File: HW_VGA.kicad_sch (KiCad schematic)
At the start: 3 parts, among them U1 25.175 MHz, U301 GAL22V10

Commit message: start working on VRAM/read logic
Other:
- added sheet ReadVRAM (ReadVRAM.kicad_sch)
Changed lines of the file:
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@@
+	)
+	(sheet
+		(at 93.98 116.84)
+		(size 27.94 45.72)
+		(fields_autoplaced yes)
+		(stroke
+			(width 0.1524)
+			(type solid)
+		)
+		(fill
+			(color 0 0 0 0.0000)
+		)
+		(property "Sheetname" "ReadVRAM"
+			(at 93.98 116.1284 0)
+			(effects
+				(font
+					(size 1.27 1.27)
+				)
+				(justify left bottom)
+			)
+		)
+		(property "Sheetfile" "ReadVRAM.kicad_sch"
+			(at 93.98 163.1446 0)
+			(effects
+				(font
+					(size 1.27 1.27)
+				)
+				(justify left top)
+			)
+		)
+		(instances
+			(project "HW_VGA"
+				(path "/c4bd4b39-993a-4195-805f-b4de6fa4aea5"
+					(page "7")
+				)
+			)
+		)
 	)
 	(sheet

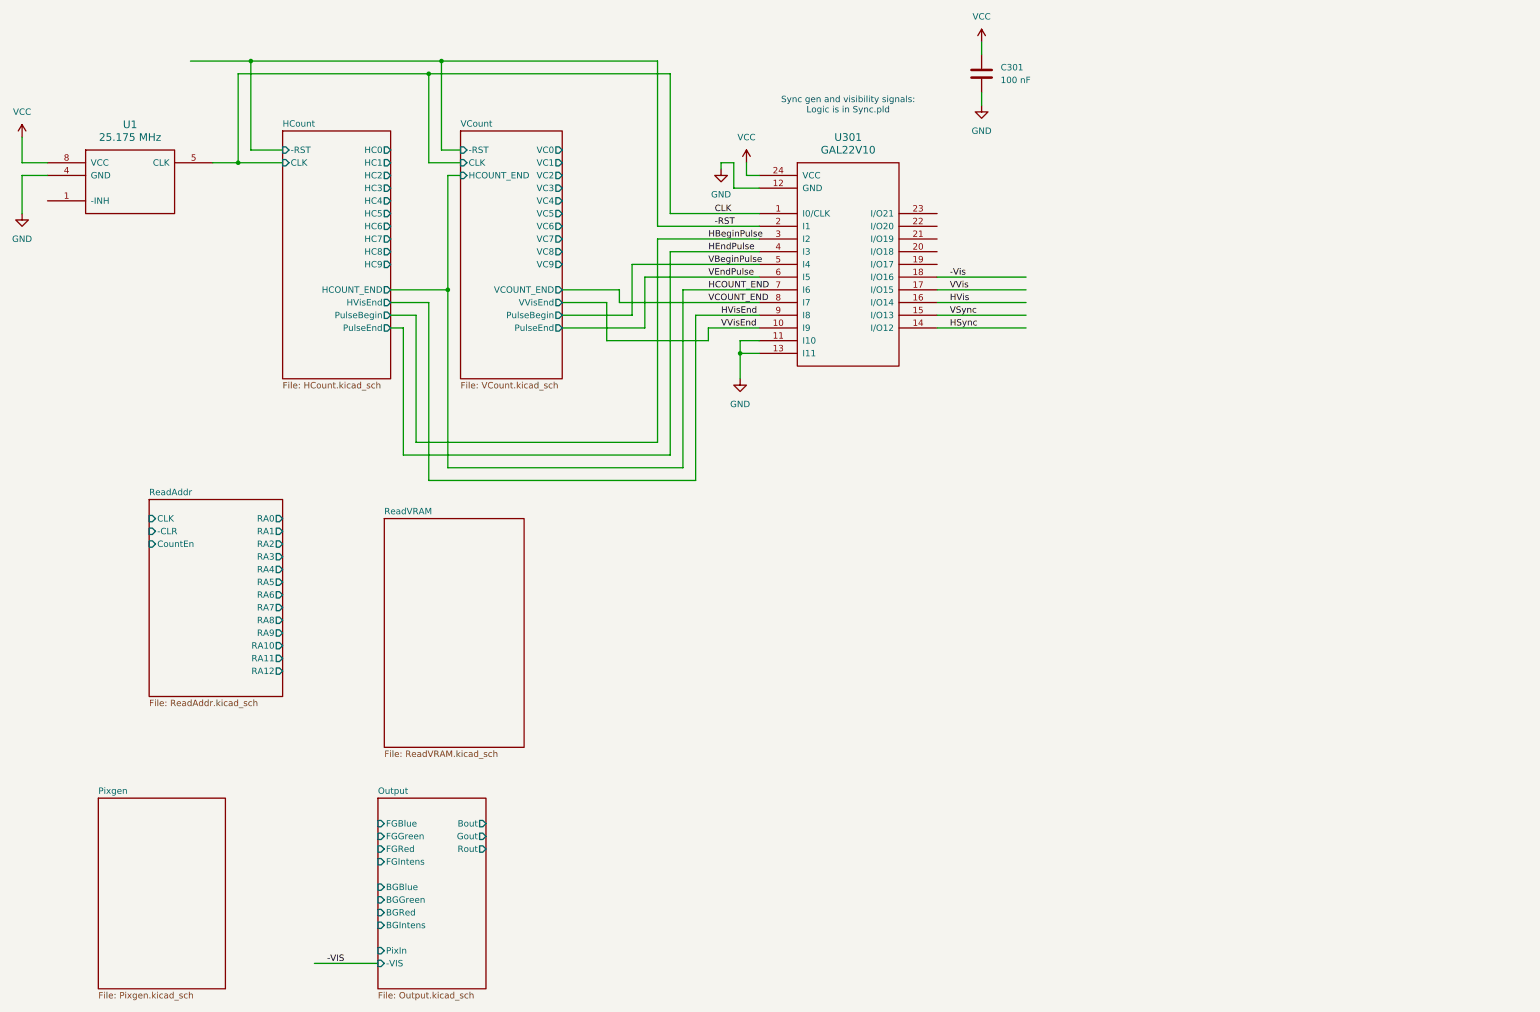
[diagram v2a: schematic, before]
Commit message: update Output circuit to use '574 as output reg
I think it makes sense to have a register for the
color signal output.
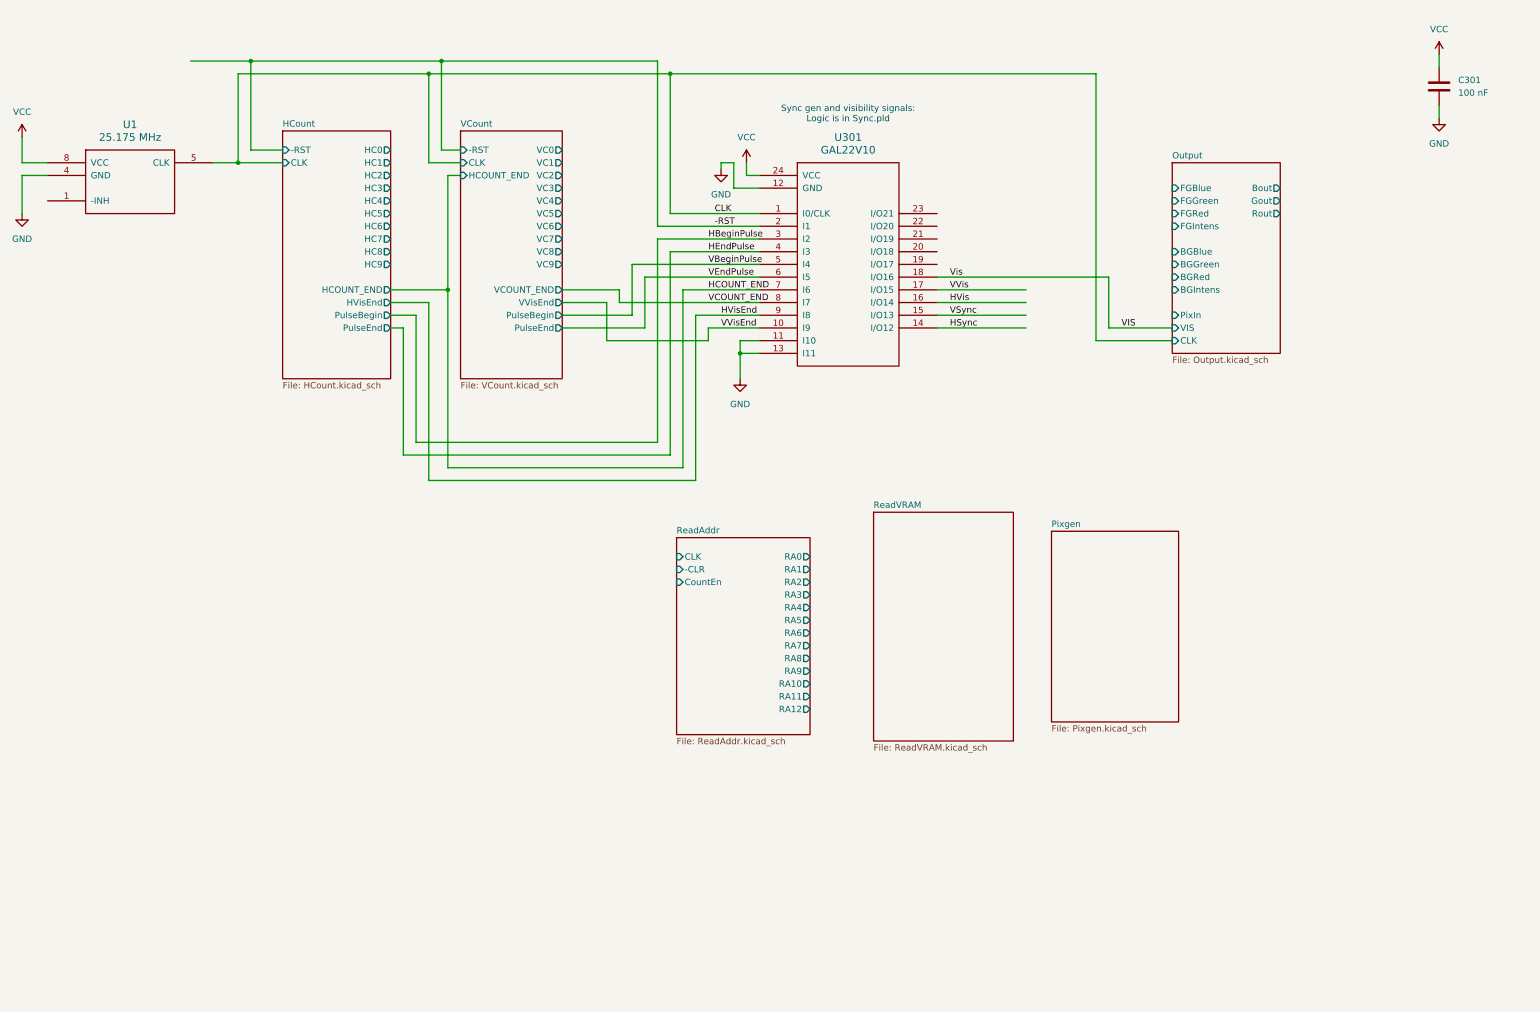
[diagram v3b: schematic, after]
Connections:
- net -Vis renamed VIS
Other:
- sheet Output ports: added CLK, VIS; removed -VIS
- moved on the sheet: C301

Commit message: make -VIS active-low again
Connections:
- net VIS renamed -Vis
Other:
- sheet Output ports: added -VIS; removed VIS
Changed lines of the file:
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@@
 		)
 	)
-	(label "VIS"
+	(label "-Vis"
 		(at 241.3 78.74 0)
 		(fields_autoplaced yes)
@@
 		)
 	)
-	(label "Vis"
+	(label "-Vis"
 		(at 207.01 68.58 0)
 		(fields_autoplaced yes)
@@
 			)
 		)
-		(pin "VIS" input
-			(at 251.46 78.74 180)
-			(effects
-				(font
-					(size 1.27 1.27)
-				)
-				(justify left)
-			)
-		)
 		(pin "CLK" input
 			(at 251.46 81.28 180)
 			(effects
 				(font
+					(size 1.27 1.27)
+				)
+				(justify left)
+			)
+		)
+		(pin "-VIS" input
+			(at 251.46 78.74 180)
+			(effects
+				(font

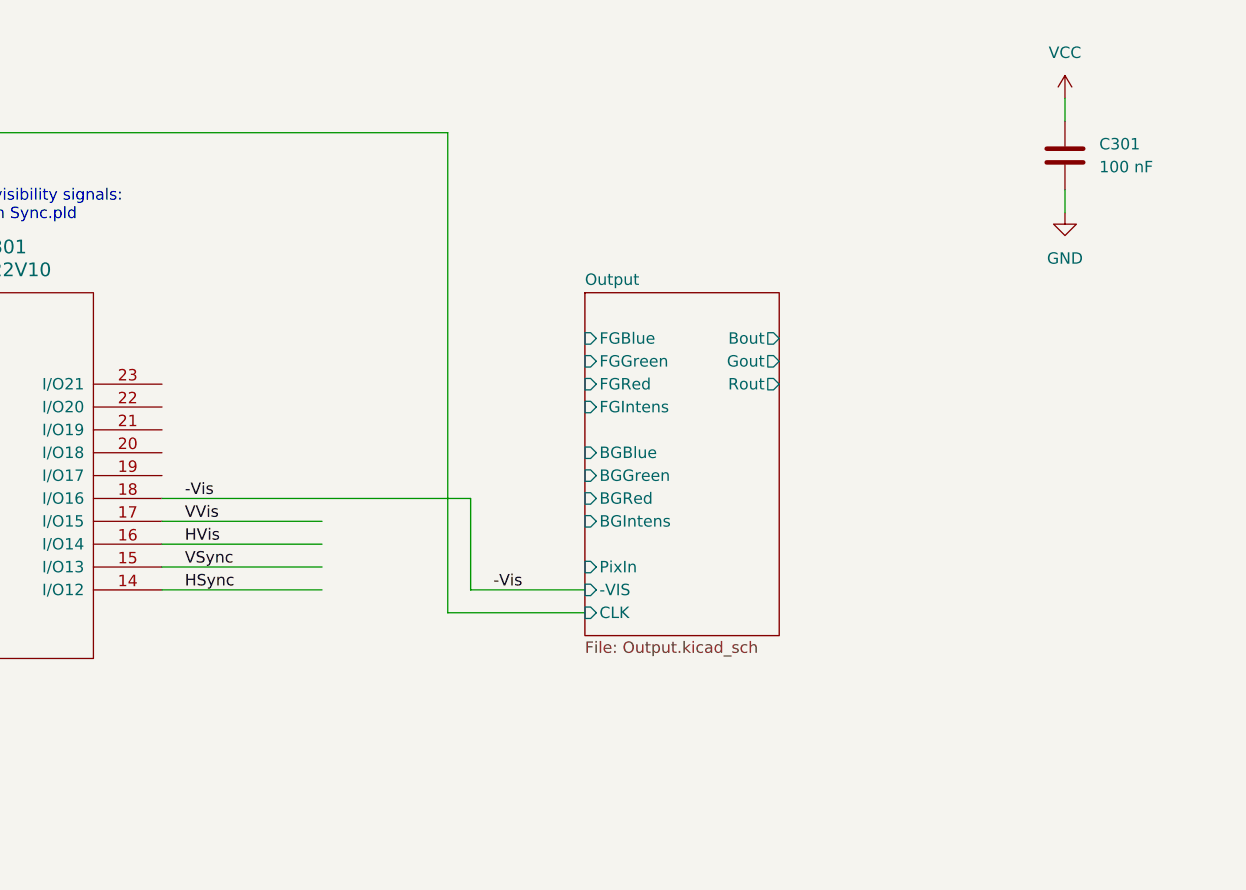
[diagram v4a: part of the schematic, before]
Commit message: use outpt reg for HSync and VSync
This will ensure that they are generated in sync with
the color outputs.

Also, added an output connector for the generated
VGA signals, and fixed the inputs to the resistor DAC.
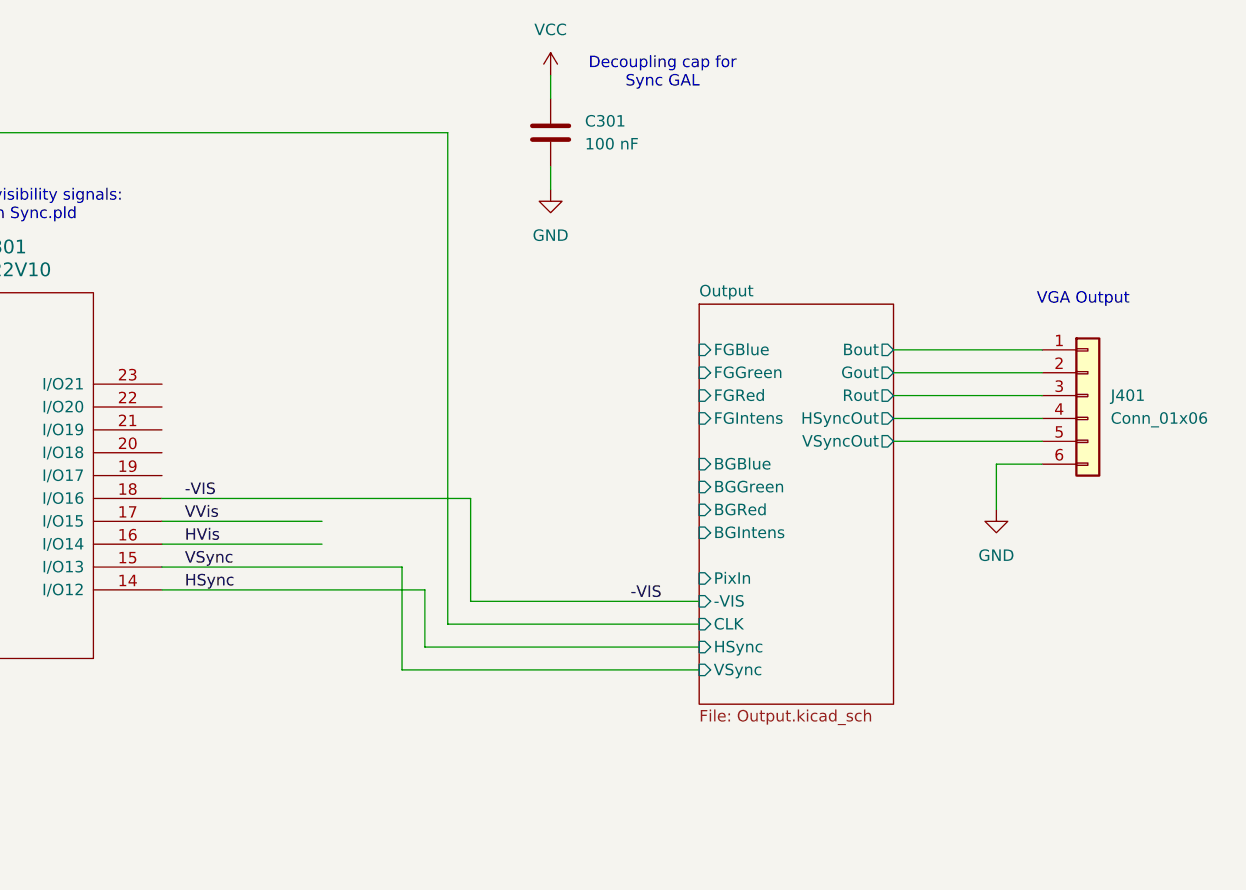
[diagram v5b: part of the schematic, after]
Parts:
- added J401: Conn_01x06, symbol Connector_Generic:Conn_01x06
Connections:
- net GND: now also J401.6 (Pin_6)
- net Output/Bout: now also J401.1 (Pin_1)
- net Output/Gout: now also J401.2 (Pin_2)
- net Output/Rout: now also J401.3 (Pin_3)
- net -Vis renamed -VIS
- new net Output/HSyncOut: J401.4 (Pin_4)
- new net Output/VSyncOut: J401.5 (Pin_5)
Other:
- sheet Output ports: added HSync, HSyncOut, VSync, VSyncOut; removed none
- note added: "Decoupling cap for Sync GAL"
- note added: "VGA Output"
- moved on the sheet: C301

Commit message: starting to work on VRAM module design
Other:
- added sheet VRAM (VRAM.kicad_sch)
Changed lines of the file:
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@@
+	)
+	(sheet
+		(at 101.6 120.65)
+		(size 27.94 39.37)
+		(fields_autoplaced yes)
+		(stroke
+			(width 0.1524)
+			(type solid)
+		)
+		(fill
+			(color 0 0 0 0.0000)
+		)
+		(property "Sheetname" "VRAM"
+			(at 101.6 119.9384 0)
+			(effects
+				(font
+					(size 1.27 1.27)
+				)
+				(justify left bottom)
+			)
+		)
+		(property "Sheetfile" "VRAM.kicad_sch"
+			(at 101.6 160.6046 0)
+			(effects
+				(font
+					(size 1.27 1.27)
+				)
+				(justify left top)
+			)
+		)
+		(instances
+			(project "HW_VGA"
+				(path "/c4bd4b39-993a-4195-805f-b4de6fa4aea5"
+					(page "8")
+				)
+			)
+		)
 	)
 	(sheet
